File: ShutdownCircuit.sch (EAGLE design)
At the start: 27 parts

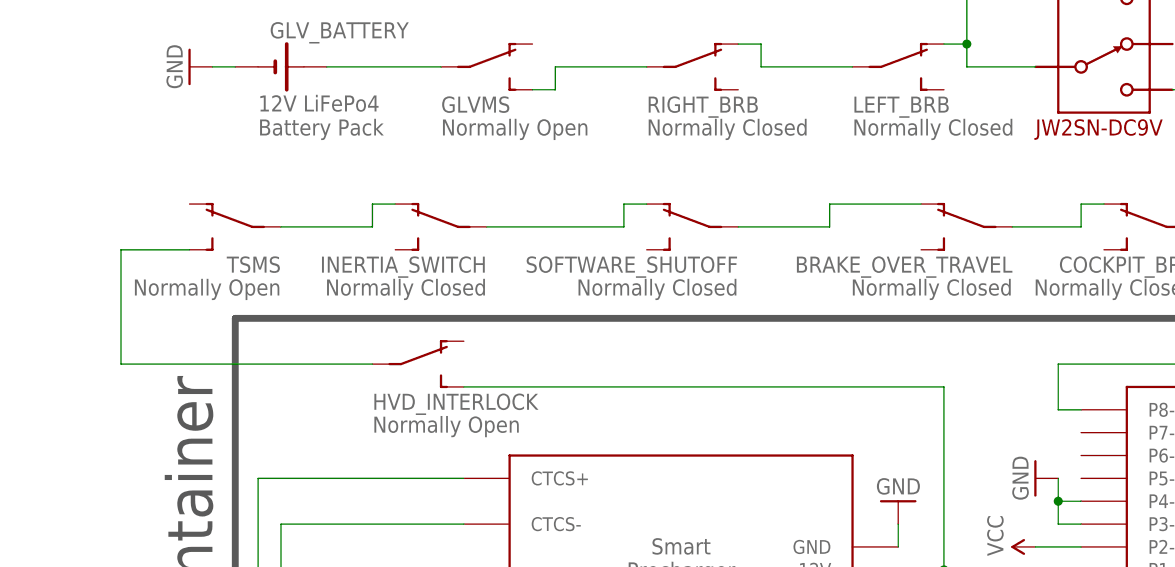
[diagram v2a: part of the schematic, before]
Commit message: Add BSPD and cleanup shutdown circuit
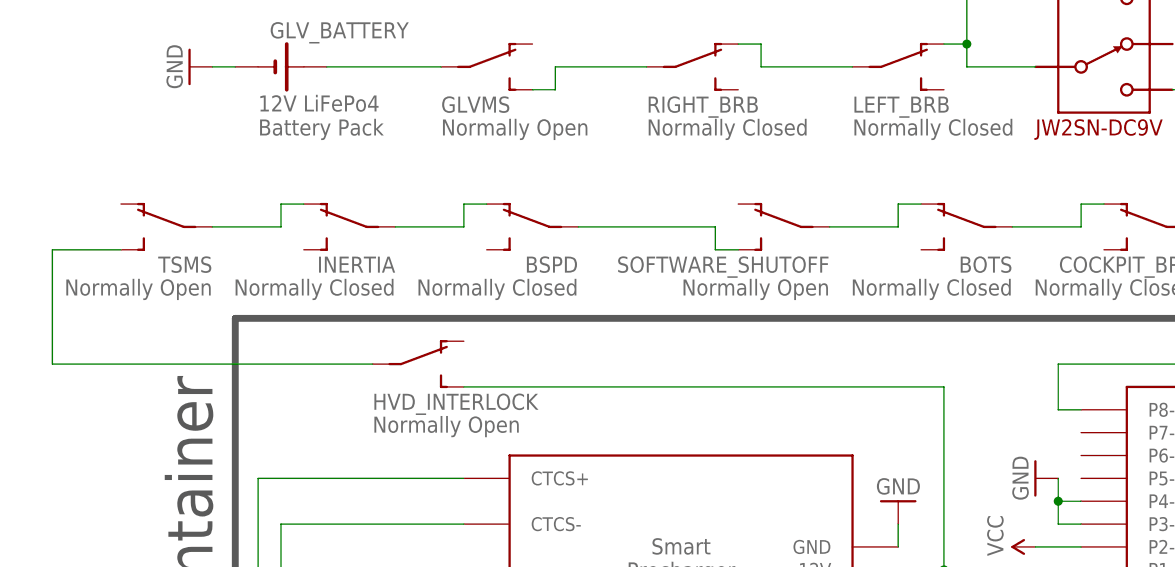
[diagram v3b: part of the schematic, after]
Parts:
- removed INERTIA_SWITCH: Normally Closed, HyTechSymbols:SWITCH_SPST
- added BSPD, INERTIA: Normally Closed, HyTechSymbols:SWITCH_SPST
- SOFTWARE_SHUTOFF: value Normally Closed -> Normally Open
- renumbered BRAKE_OVER_TRAVEL to BOTS
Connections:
- new net N$17: BSPD.O, INERTIA.P
- net N$11: now also INERTIA.O; no longer INERTIA_SWITCH.O
- net N$7: now also BSPD.P, SOFTWARE_SHUTOFF.S; no longer INERTIA_SWITCH.P, SOFTWARE_SHUTOFF.O
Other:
- moved on the sheet: SOFTWARE_SHUTOFF, TSMS
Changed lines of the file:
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@@
 <part name="GND2" library="HyTechSymbols" deviceset="GND" device=""/>
 <part name="COCKPIT_BRB" library="HyTechSymbols" deviceset="SWITCH_SPST" device="" value="Normally Closed"/>
-<part name="INERTIA_SWITCH" library="HyTechSymbols" deviceset="SWITCH_SPST" device="" value="Normally Closed"/>
-<part name="BRAKE_OVER_TRAVEL" library="HyTechSymbols" deviceset="SWITCH_SPST" device="" value="Normally Closed"/>
+<part name="INERTIA" library="HyTechSymbols" deviceset="SWITCH_SPST" device="" value="Normally Closed"/>
+<part name="BOTS" library="HyTechSymbols" deviceset="SWITCH_SPST" device="" value="Normally Closed"/>
 <part name="TSMS" library="HyTechSymbols" deviceset="SWITCH_SPST" device="" value="Normally Open"/>
 <part name="HVD_INTERLOCK" library="HyTechSymbols" deviceset="SWITCH_SPST" device="" value="Normally Open"/>
@@
 <part name="GLV_SYSTEMS1" library="HyTechSymbols" deviceset="VIN" device="" value="VCC"/>
 <part name="GND9" library="HyTechSymbols" deviceset="GND" device=""/>
-<part name="SOFTWARE_SHUTOFF" library="HyTechSymbols" deviceset="SWITCH_SPST" device="" value="Normally Closed"/>
+<part name="SOFTWARE_SHUTOFF" library="HyTechSymbols" deviceset="SWITCH_SPST" device="" value="Normally Open"/>
+<part name="BSPD" library="HyTechSymbols" deviceset="SWITCH_SPST" device="" value="Normally Closed"/>
 </parts>
 <sheets>
@@
 <instance part="GND2" gate="1" x="88.9" y="50.8" rot="R270"/>
 <instance part="COCKPIT_BRB" gate="SPST" x="101.6" y="91.44" rot="MR270"/>
-<instance part="INERTIA_SWITCH" gate="SPST" x="22.86" y="91.44" rot="MR270"/>
-<instance part="BRAKE_OVER_TRAVEL" gate="SPST" x="81.28" y="91.44" rot="MR270"/>
-<instance part="TSMS" gate="SPST" x="0" y="91.44" rot="MR270"/>
+<instance part="INERTIA" gate="SPST" x="12.7" y="91.44" rot="MR270"/>
+<instance part="BOTS" gate="SPST" x="81.28" y="91.44" rot="MR270"/>
+<instance part="TSMS" gate="SPST" x="-7.62" y="91.44" rot="MR270"/>
 <instance part="HVD_INTERLOCK" gate="SPST" x="20.32" y="76.2" rot="R270"/>
 <instance part="SEGMENT1" gate="G$1" x="30.48" y="17.78" rot="R90"/>
@@
 <instance part="GLV_SYSTEMS1" gate="G$1" x="88.9" y="55.88" rot="R90"/>
 <instance part="GND9" gate="1" x="88.9" y="63.5" rot="R270"/>
-<instance part="SOFTWARE_SHUTOFF" gate="SPST" x="50.8" y="91.44" rot="MR270"/>
+<instance part="SOFTWARE_SHUTOFF" gate="SPST" x="60.96" y="91.44" rot="MR270"/>
+<instance part="BSPD" gate="SPST" x="33.02" y="91.44" rot="MR270"/>
 </instances>
 <busses>
@@
 <wire x1="96.52" y1="93.98" x2="93.98" y2="93.98" width="0.1524" layer="91"/>
 <wire x1="93.98" y1="93.98" x2="93.98" y2="91.44" width="0.1524" layer="91"/>
-<pinref part="BRAKE_OVER_TRAVEL" gate="SPST" pin="P"/>
+<pinref part="BOTS" gate="SPST" pin="P"/>
 <wire x1="93.98" y1="91.44" x2="86.36" y2="91.44" width="0.1524" layer="91"/>
 </segment>
@@
 <net name="N$10" class="0">
 <segment>
-<pinref part="BRAKE_OVER_TRAVEL" gate="SPST" pin="O"/>
-<wire x1="76.2" y1="93.98" x2="66.04" y2="93.98" width="0.1524" layer="91"/>
-<wire x1="66.04" y1="93.98" x2="66.04" y2="91.44" width="0.1524" layer="91"/>
+<pinref part="BOTS" gate="SPST" pin="O"/>
+<wire x1="76.2" y1="93.98" x2="73.66" y2="93.98" width="0.1524" layer="91"/>
+<wire x1="73.66" y1="93.98" x2="73.66" y2="91.44" width="0.1524" layer="91"/>
 <pinref part="SOFTWARE_SHUTOFF" gate="SPST" pin="P"/>
-<wire x1="66.04" y1="91.44" x2="55.88" y2="91.44" width="0.1524" layer="91"/>
+<wire x1="73.66" y1="91.44" x2="66.04" y2="91.44" width="0.1524" layer="91"/>
 </segment>
 </net>
 <net name="N$11" class="0">
 <segment>
-<pinref part="INERTIA_SWITCH" gate="SPST" pin="O"/>
-<wire x1="17.78" y1="93.98" x2="15.24" y2="93.98" width="0.1524" layer="91"/>
-<wire x1="15.24" y1="93.98" x2="15.24" y2="91.44" width="0.1524" layer="91"/>
+<pinref part="INERTIA" gate="SPST" pin="O"/>
+<wire x1="7.62" y1="93.98" x2="5.08" y2="93.98" width="0.1524" layer="91"/>
+<wire x1="5.08" y1="93.98" x2="5.08" y2="91.44" width="0.1524" layer="91"/>
 <pinref part="TSMS" gate="SPST" pin="P"/>
-<wire x1="15.24" y1="91.44" x2="5.08" y2="91.44" width="0.1524" layer="91"/>
+<wire x1="5.08" y1="91.44" x2="-2.54" y2="91.44" width="0.1524" layer="91"/>
 </segment>
 </net>
@@
 <segment>
 <pinref part="TSMS" gate="SPST" pin="S"/>
-<wire x1="-5.08" y1="88.9" x2="-12.7" y2="88.9" width="0.1524" layer="91"/>
-<wire x1="-12.7" y1="88.9" x2="-12.7" y2="76.2" width="0.1524" layer="91"/>
+<wire x1="-12.7" y1="88.9" x2="-20.32" y2="88.9" width="0.1524" layer="91"/>
+<wire x1="-20.32" y1="88.9" x2="-20.32" y2="76.2" width="0.1524" layer="91"/>
 <pinref part="HVD_INTERLOCK" gate="SPST" pin="P"/>
-<wire x1="-12.7" y1="76.2" x2="15.24" y2="76.2" width="0.1524" layer="91"/>
+<wire x1="-20.32" y1="76.2" x2="15.24" y2="76.2" width="0.1524" layer="91"/>
 </segment>
 </net>
@@
 <net name="N$7" class="0">
 <segment>
-<pinref part="INERTIA_SWITCH" gate="SPST" pin="P"/>
-<wire x1="27.94" y1="91.44" x2="43.18" y2="91.44" width="0.1524" layer="91"/>
-<wire x1="43.18" y1="91.44" x2="43.18" y2="93.98" width="0.1524" layer="91"/>
-<pinref part="SOFTWARE_SHUTOFF" gate="SPST" pin="O"/>
-<wire x1="43.18" y1="93.98" x2="45.72" y2="93.98" width="0.1524" layer="91"/>
-</segment>
-</net>
+<pinref part="BSPD" gate="SPST" pin="P"/>
+<wire x1="53.34" y1="91.44" x2="38.1" y2="91.44" width="0.1524" layer="91"/>
+<wire x1="53.34" y1="91.44" x2="53.34" y2="88.9" width="0.1524" layer="91"/>
+<pinref part="SOFTWARE_SHUTOFF" gate="SPST" pin="S"/>
+<wire x1="53.34" y1="88.9" x2="55.88" y2="88.9" width="0.1524" layer="91"/>
+</segment>
+</net>
+<net name="N$17" class="0">
+<segment>
+<pinref part="BSPD" gate="SPST" pin="O"/>
+<wire x1="27.94" y1="93.98" x2="25.4" y2="93.98" width="0.1524" layer="91"/>
+<wire x1="25.4" y1="93.98" x2="25.4" y2="91.44" width="0.1524" layer="91"/>
+<pinref part="INERTIA" gate="SPST" pin="P"/>
+<wire x1="25.4" y1="91.44" x2="17.78" y2="91.44" width="0.1524" layer="91"/>
+</segment>
+</net>

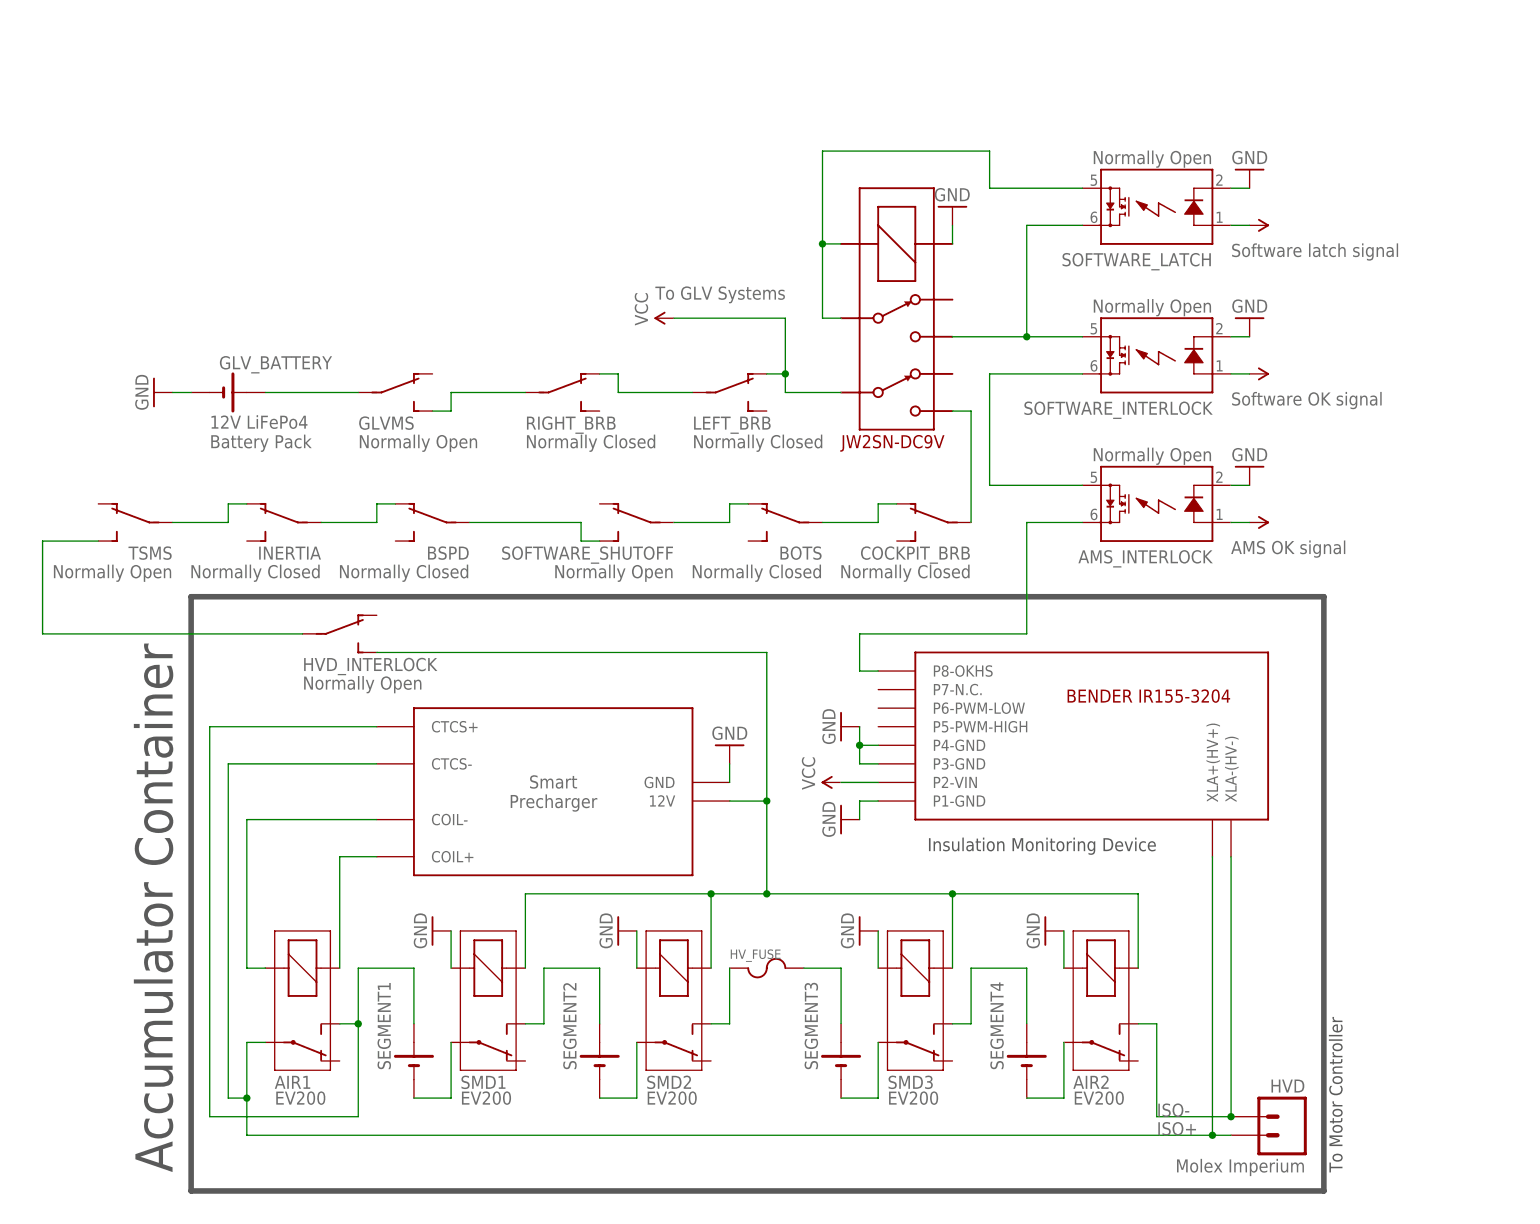
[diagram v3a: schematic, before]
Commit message: Update smart precharger symbol, add crash sensor symbol, update shutdown circuit
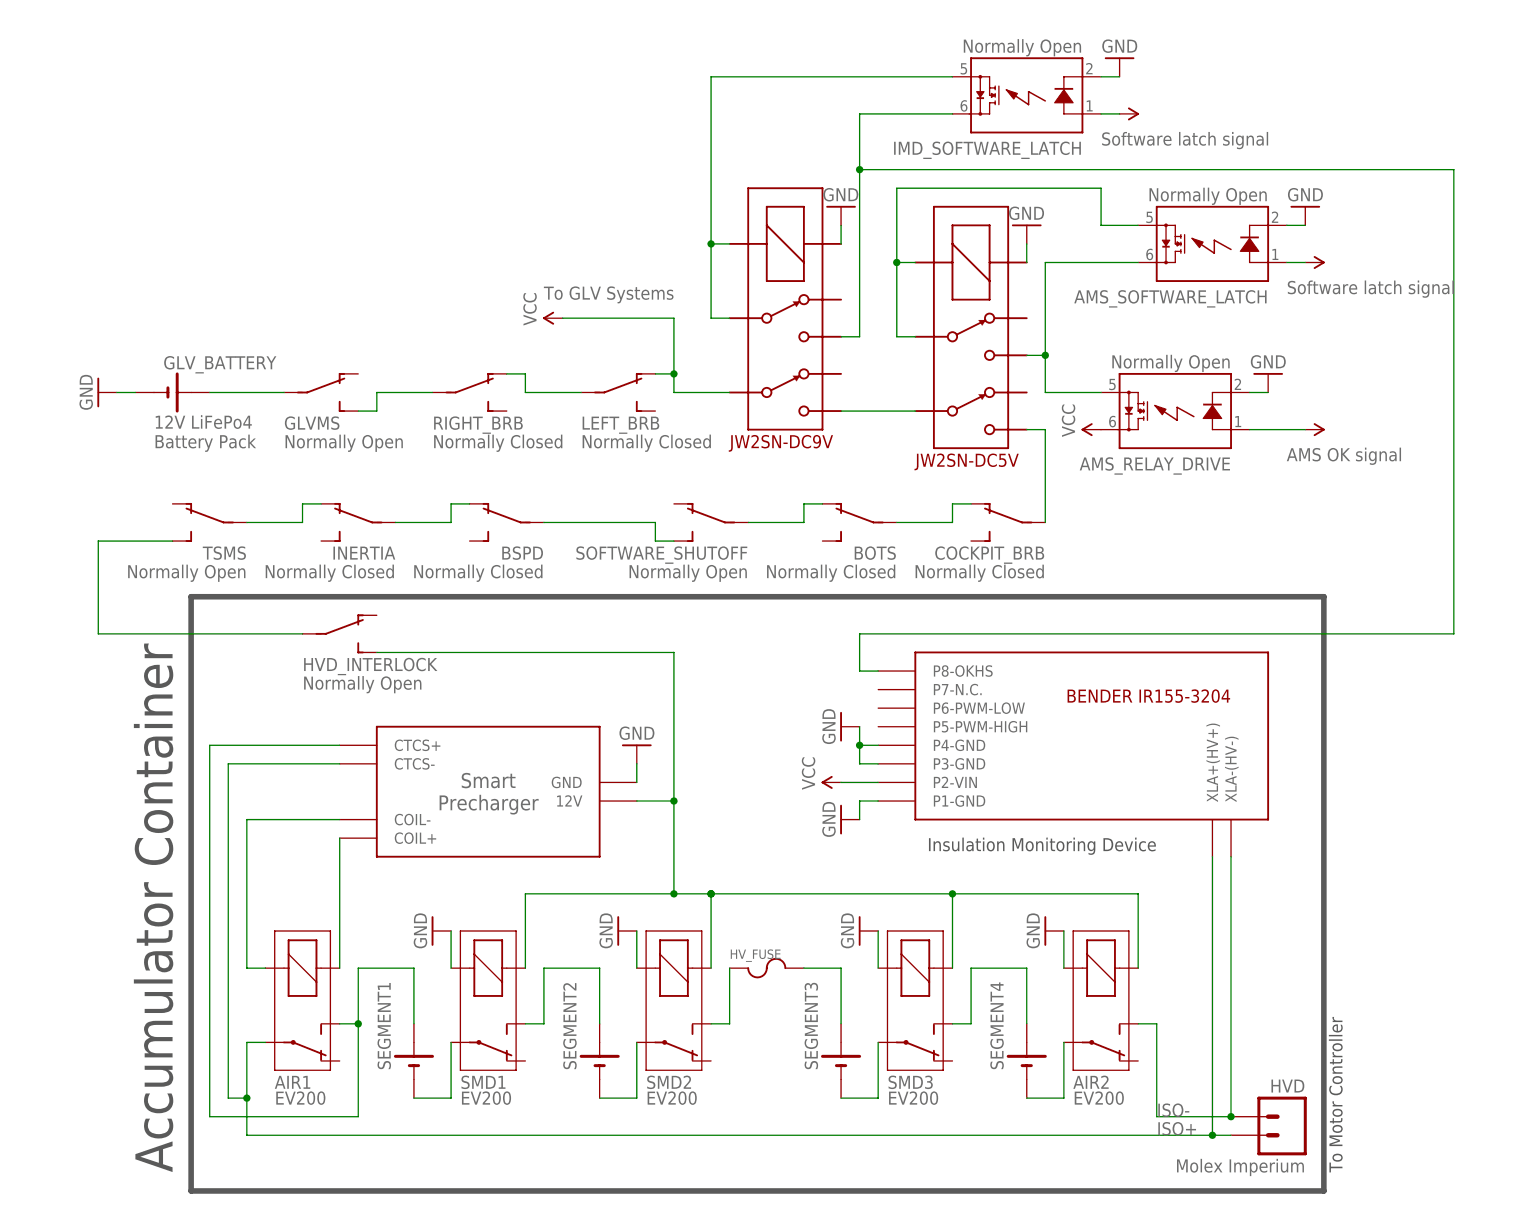
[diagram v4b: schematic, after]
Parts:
- removed AMS_INTERLOCK, SOFTWARE_INTERLOCK, SOFTWARE_LATCH: Normally Open, HyTechDevices:SOLID_STATE_RELAY_VO14642AT
- added AMS_RELAY_DRIVE, AMS_SOFTWARE_LATCH, IMD_SOFTWARE_LATCH: Normally Open, HyTechDevices:SOLID_STATE_RELAY_VO14642AT
- added U$4: DPDT_RELAY_PANASONIC_JW2SN-DC5V, HyTechDevices:DPDT_RELAY_PANASONIC_JW2SN-DC5V
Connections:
- net GND: now also AMS_RELAY_DRIVE.LED-, AMS_SOFTWARE_LATCH.LED-, IMD_SOFTWARE_LATCH.LED-, U$4.COIL+; no longer AMS_INTERLOCK.LED-, SOFTWARE_INTERLOCK.LED-, SOFTWARE_LATCH.LED-
- net N$13: now also AMS_RELAY_DRIVE.IO2, AMS_SOFTWARE_LATCH.IO1, U$4.4; no longer AMS_INTERLOCK.LED+
- net N$16: now also AMS_SOFTWARE_LATCH.IO2, U$4.3, U$4.COIL-; no longer AMS_INTERLOCK.IO1, U$2.P8-OKHS
- net N$4: now also IMD_SOFTWARE_LATCH.IO1, U$2.P8-OKHS; no longer SOFTWARE_INTERLOCK.IO2, SOFTWARE_LATCH.IO1
- net N$5: now also U$1.5, U$4.6; no longer AMS_INTERLOCK.IO2, SOFTWARE_INTERLOCK.IO1
- net N$6: now also IMD_SOFTWARE_LATCH.IO2; no longer SOFTWARE_LATCH.IO2
- net N$8: now also U$4.5; no longer U$1.5
- net VIN: now also AMS_RELAY_DRIVE.IO1, AMS_RELAY_DRIVE.LED+, AMS_SOFTWARE_LATCH.LED+, IMD_SOFTWARE_LATCH.LED+; no longer SOFTWARE_INTERLOCK.LED+, SOFTWARE_LATCH.LED+
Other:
- note removed: "Software OK signal"
- moved on the sheet: BOTS, BSPD, COCKPIT_BRB, GLVMS, GLV_BATTERY, INERTIA, LEFT_BRB, RIGHT_BRB, SOFTWARE_SHUTOFF, TSMS
